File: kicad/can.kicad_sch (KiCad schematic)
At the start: 16 parts, among them IC1 TCAN3403DRQ1, IC3 ADM3050EBRIZ-RL, J3 Conn_01x02, J8 Conn_01x04, Q2 2N7002, Q3 2N7002

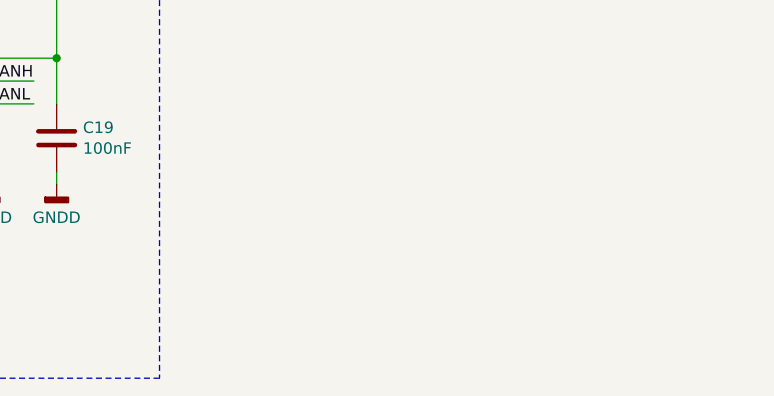
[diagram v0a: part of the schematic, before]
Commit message: Fixed power issue
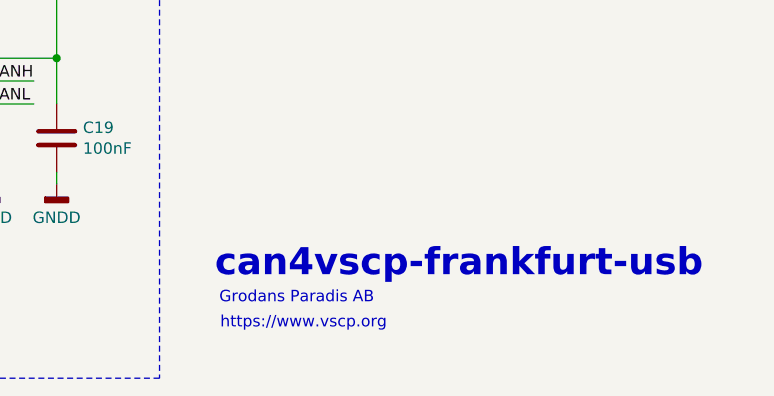
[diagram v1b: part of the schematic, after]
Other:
- note added: "Grodans Paradis AB"
- note added: "can4vscp-frankfurt-usb"
- note added: "https://www.vscp.org"
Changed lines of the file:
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@@
+		)
+	)
+	(text "https://www.vscp.org"
+		(exclude_from_sim no)
+		(at 189.992 176.784 0)
+		(effects
+			(font
+				(size 1.27 1.27)
+			)
 		)
 	)
@@
 		(effects
 			(font
+				(size 1.27 1.27)
+			)
+		)
+	)
+	(text "can4vscp-frankfurt-usb"
+		(exclude_from_sim no)
+		(at 207.264 170.18 0)
+		(effects
+			(font
+				(size 3 3)
+				(thickness 0.6)
+				(bold yes)
+			)
+		)
+	)
+	(text "Grodans Paradis AB"
+		(exclude_from_sim no)
+		(at 189.23 173.99 0)
+		(effects
+			(font

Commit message: Reversion A schema and PCB
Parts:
- IC2: renamed from IC1; footprint SOIC127P600X175-8N -> TCAN3403DRQ1:SOIC127P600X175-8N
- IC3: footprint SOIC127P1031X265-8N -> TCAN3403DRQ1:SOIC127P600X175-8N
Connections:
- net +3V3 renamed +3.3V
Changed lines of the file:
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@@
 			)
 		)
-		(property "Footprint" "SOIC127P1031X265-8N"
+		(property "Footprint" "TCAN3403DRQ1:SOIC127P600X175-8N"
 			(at 148.59 242.24 0)
 			(hide yes)
@@
 		(dnp no)
 		(fields_autoplaced yes)
-		(property "Reference" "IC1"
+		(property "Reference" "IC2"
 			(at 88.9 54.2755 0)
 			(show_name no)
@@
 			)
 		)
-		(property "Footprint" "SOIC127P600X175-8N"
+		(property "Footprint" "TCAN3403DRQ1:SOIC127P600X175-8N"
 			(at 101.6 155.88 0)
 			(hide yes)
@@
 			(project "vscp-din-stm32h552-can-z102"
 				(path "/a1545928-1195-40b9-b3c4-78f837012afb/494e770b-b0f3-49c9-9124-5b490db174bf"
-					(reference "IC1")
+					(reference "IC2")
 					(unit 1)
 				)
@@
 	)
 	(symbol
-		(lib_id "power:+3.3V")
-		(at 36.83 31.75 0)
-		(unit 1)
-		(body_style 1)
-		(exclude_from_sim no)
-		(in_bom yes)
-		(on_board yes)
-		(in_pos_files yes)
-		(dnp no)
-		(fields_autoplaced yes)
-		(property "Reference" "#PWR0139"
-			(at 36.83 35.56 0)
-			(hide yes)
-			(show_name no)
-			(do_not_autoplace no)
-			(effects
-				(font
-					(size 1.27 1.27)
-				)
-			)
-		)
-		(property "Value" "+3V3"
-			(at 36.83 28.1742 0)
-			(show_name no)
-			(do_not_autoplace no)
-			(effects
-				(font
-					(size 1.27 1.27)
-				)
-			)
-		)
-		(property "Footprint" ""
-			(at 36.83 31.75 0)
-			(hide yes)
-			(show_name no)
-			(do_not_autoplace no)
-			(effects
-				(font
-					(size 1.27 1.27)
-				)
-			)
-		)
-		(property "Datasheet" ""
-			(at 36.83 31.75 0)
-			(hide yes)
-			(show_name no)
-			(do_not_autoplace no)
-			(effects
-				(font
-					(size 1.27 1.27)
-				)
-			)
-		)
-		(property "Description" "Power symbol creates a global label with name \"+3.3V\""
-			(at 36.83 31.75 0)
-			(hide yes)
-			(show_name no)
-			(do_not_autoplace no)
-			(effects
-				(font
-					(size 1.27 1.27)
-				)
-			)
-		)
-		(pin "1"
-		)
-		(instances
-			(project "vscp-din-stm32h552-can-z102"
-				(path "/a1545928-1195-40b9-b3c4-78f837012afb/494e770b-b0f3-49c9-9124-5b490db174bf"
-					(reference "#PWR0139")
-					(unit 1)
-				)
-			)
-		)
-	)
-	(symbol
 		(lib_id "powerport:+5V")
 		(at 25.4 142.24 0)
@@
 					(unit 1)
 				)
+			)
+		)
+	)
+	(symbol
+		(lib_id "power:+3.3V")
+		(at 36.83 31.75 0)
+		(unit 1)
+		(body_style 1)
+		(exclude_from_sim no)
+		(in_bom yes)
+		(on_board yes)
+		(in_pos_files yes)
+		(dnp no)
+		(fields_autoplaced yes)
+		(property "Reference" "#PWR041"
+			(at 36.83 35.56 0)
+			(hide yes)
+			(show_name no)
+			(do_not_autoplace no)
+			(effects
+				(font
+					(size 1.27 1.27)
+				)
+			)
+		)
+		(property "Value" "+3.3V"
+			(at 36.83 27.6169 0)
+			(show_name no)
+			(do_not_autoplace no)
+			(effects
+				(font
+					(size 1.27 1.27)
+				)
+			)
+		)
+		(property "Footprint" ""
+			(at 36.83 31.75 0)
+			(hide yes)
+			(show_name no)
+			(do_not_autoplace no)
+			(effects
+				(font
+					(size 1.27 1.27)
+				)
+			)
+		)
+		(property "Datasheet" ""
+			(at 36.83 31.75 0)
+			(hide yes)
+			(show_name no)
+			(do_not_autoplace no)
+			(effects
+				(font
+					(size 1.27 1.27)
+				)
+			)
+		)
+		(property "Description" "Power symbol creates a global label with name \"+3.3V\""
+			(at 36.83 31.75 0)
+			(hide yes)
+			(show_name no)
+			(do_not_autoplace no)
+			(effects
+				(font
+					(size 1.27 1.27)
+				)
+			)
+		)
+		(pin "1"
+		)
+		(instances
+			(project "vscp-din-stm32h552-can-z102"
+				(path "/a1545928-1195-40b9-b3c4-78f837012afb/494e770b-b0f3-49c9-9124-5b490db174bf"
+					(reference "#PWR041")
+					(unit 1)
+				)

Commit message: Fixed 3D models
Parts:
- IC3: footprint TCAN3403DRQ1:SOIC127P600X175-8N -> ADM3050EBRIZ:SOIC127P1031X265-8N
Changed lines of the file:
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@@
+	(wire
+		(pts
+			(xy 97.79 160.02) (xy 97.79 158.75)
+		)
+		(stroke
+			(width 0)
+			(type default)
+		)
+	)
 	(wire
 		(pts
@@
 			)
 		)
-		(property "Footprint" "TCAN3403DRQ1:SOIC127P600X175-8N"
+		(property "Footprint" "ADM3050EBRIZ:SOIC127P1031X265-8N"
 			(at 148.59 242.24 0)
 			(hide yes)
@@
 	(symbol
 		(lib_id "power:GND")
-		(at 97.79 158.75 0)
+		(at 97.79 160.02 0)
 		(unit 1)
 		(body_style 1)
@@
 		(dnp no)
 		(property "Reference" "#PWR0147"
-			(at 97.79 165.1 0)
+			(at 97.79 166.37 0)
 			(hide yes)
 			(show_name no)
@@
 		)
 		(property "Value" "GND"
-			(at 97.917 163.1442 0)
+			(at 97.917 164.4142 0)
 			(show_name no)
 			(do_not_autoplace no)
@@
 		)
 		(property "Footprint" ""
-			(at 97.79 158.75 0)
+			(at 97.79 160.02 0)
 			(hide yes)
 			(show_name no)
@@
 		)
 		(property "Datasheet" ""
-			(at 97.79 158.75 0)
+			(at 97.79 160.02 0)
 			(hide yes)
 			(show_name no)
@@
 		)
 		(property "Description" "Power symbol creates a global label with name \"GND\" , ground"
-			(at 97.79 158.75 0)
-			(hide yes)
-			(show_name no)
+			(at 97.79 160.02 0)
+			(hide yes)
+			(show_name no)
